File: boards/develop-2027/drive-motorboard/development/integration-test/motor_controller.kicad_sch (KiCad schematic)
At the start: 5 parts

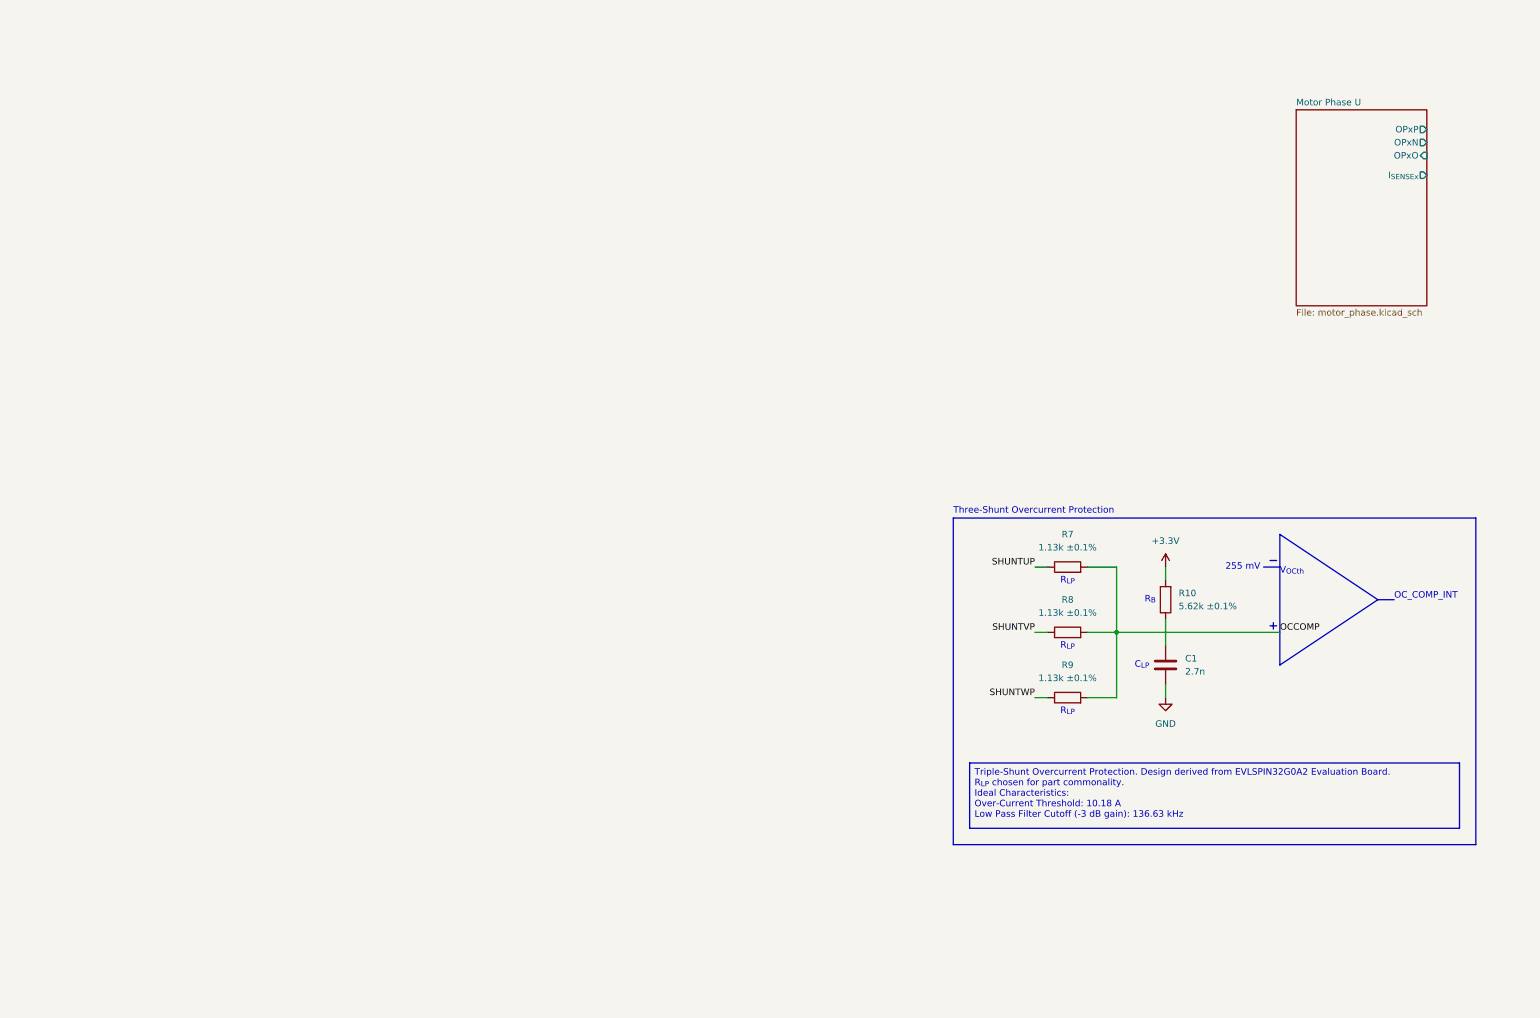
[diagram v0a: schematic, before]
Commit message: Add power stage
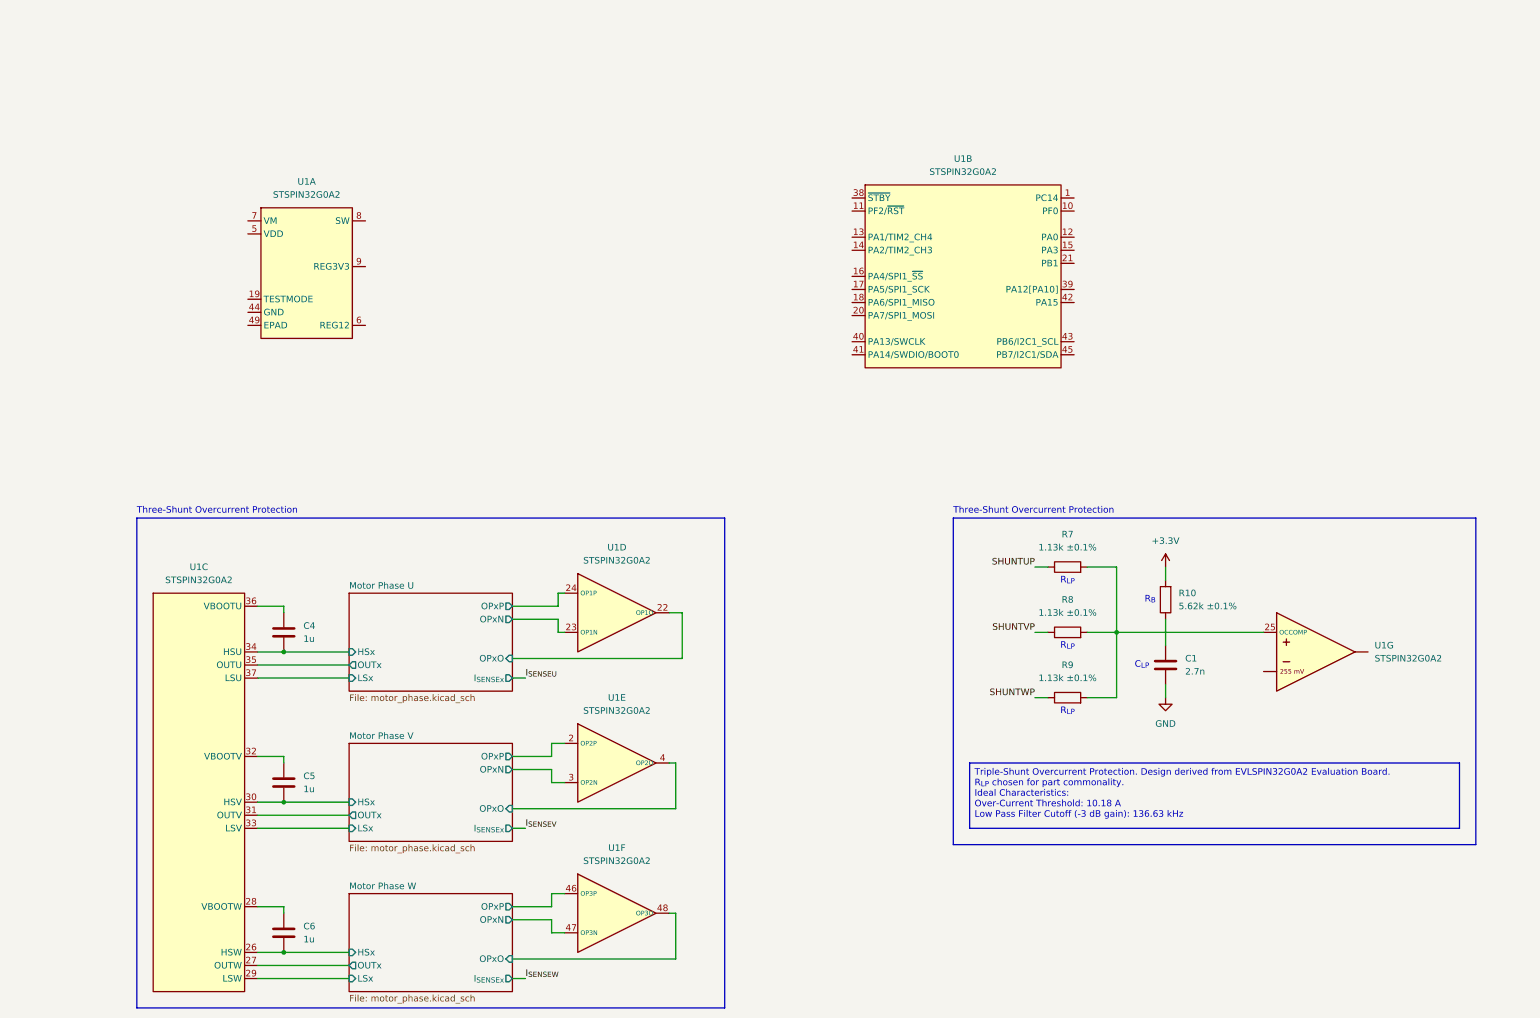
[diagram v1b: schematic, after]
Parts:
- added C4, C5, C6: 1u, Capacitor_SMD:C_0603_1608Metric, symbol Device:C
- added U1: STSPIN32G0A2, Package_DFN_QFN:VQFN-48-1EP_7x7mm_P0.5mm_EP2.6x2.6mm, symbol RJ-MCU:STSPIN32G0A2
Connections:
- net Motor Phase U/OPxN: now also U1.23 (OP1N)
- net Motor Phase U/OPxO: now also U1.22 (OP1O)
- net Motor Phase U/OPxP: now also U1.24 (OP1P)
- net OCCOMP: no longer names the net of R7.2, R8.2, R9.2
- net OCCOMP: now also U1.25 (OCCOMP)
- new net: C6.1, U1.28 (VBOOTW)
- new net: C5.1, U1.32 (VBOOTV)
- new net: C4.1, U1.36 (VBOOTU)
- new net Motor Phase U/HSx: C4.2, U1.34 (HSU)
- new net Motor Phase U/LSx: U1.37 (LSU)
- new net Motor Phase U/OUTx: U1.35 (OUTU)
- new net Motor Phase V/HSx: C5.2, U1.30 (HSV)
- new net Motor Phase V/LSx: U1.33 (LSV)
- new net Motor Phase V/OPxN: U1.3 (OP2N)
- new net Motor Phase V/OPxO: U1.4 (OP2O)
- new net Motor Phase V/OPxP: U1.2 (OP2P)
- new net Motor Phase V/OUTx: U1.31 (OUTV)
- new net Motor Phase W/HSx: C6.2, U1.26 (HSW)
- new net Motor Phase W/LSx: U1.29 (LSW)
- new net Motor Phase W/OPxN: U1.47 (OP3N)
- new net Motor Phase W/OPxO: U1.48 (OP3O)
- new net Motor Phase W/OPxP: U1.46 (OP3P)
- new net Motor Phase W/OUTx: U1.27 (OUTW)
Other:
- added sheet Motor Phase V (motor_phase.kicad_sch)
- added sheet Motor Phase W (motor_phase.kicad_sch)
- sheet Motor Phase U ports: added HSx, LSx, OUTx; removed none
- note removed: "255 mV"
- note removed: "OC_COMP_INT"
- note removed: "V_{OCth}"

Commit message: Add test points
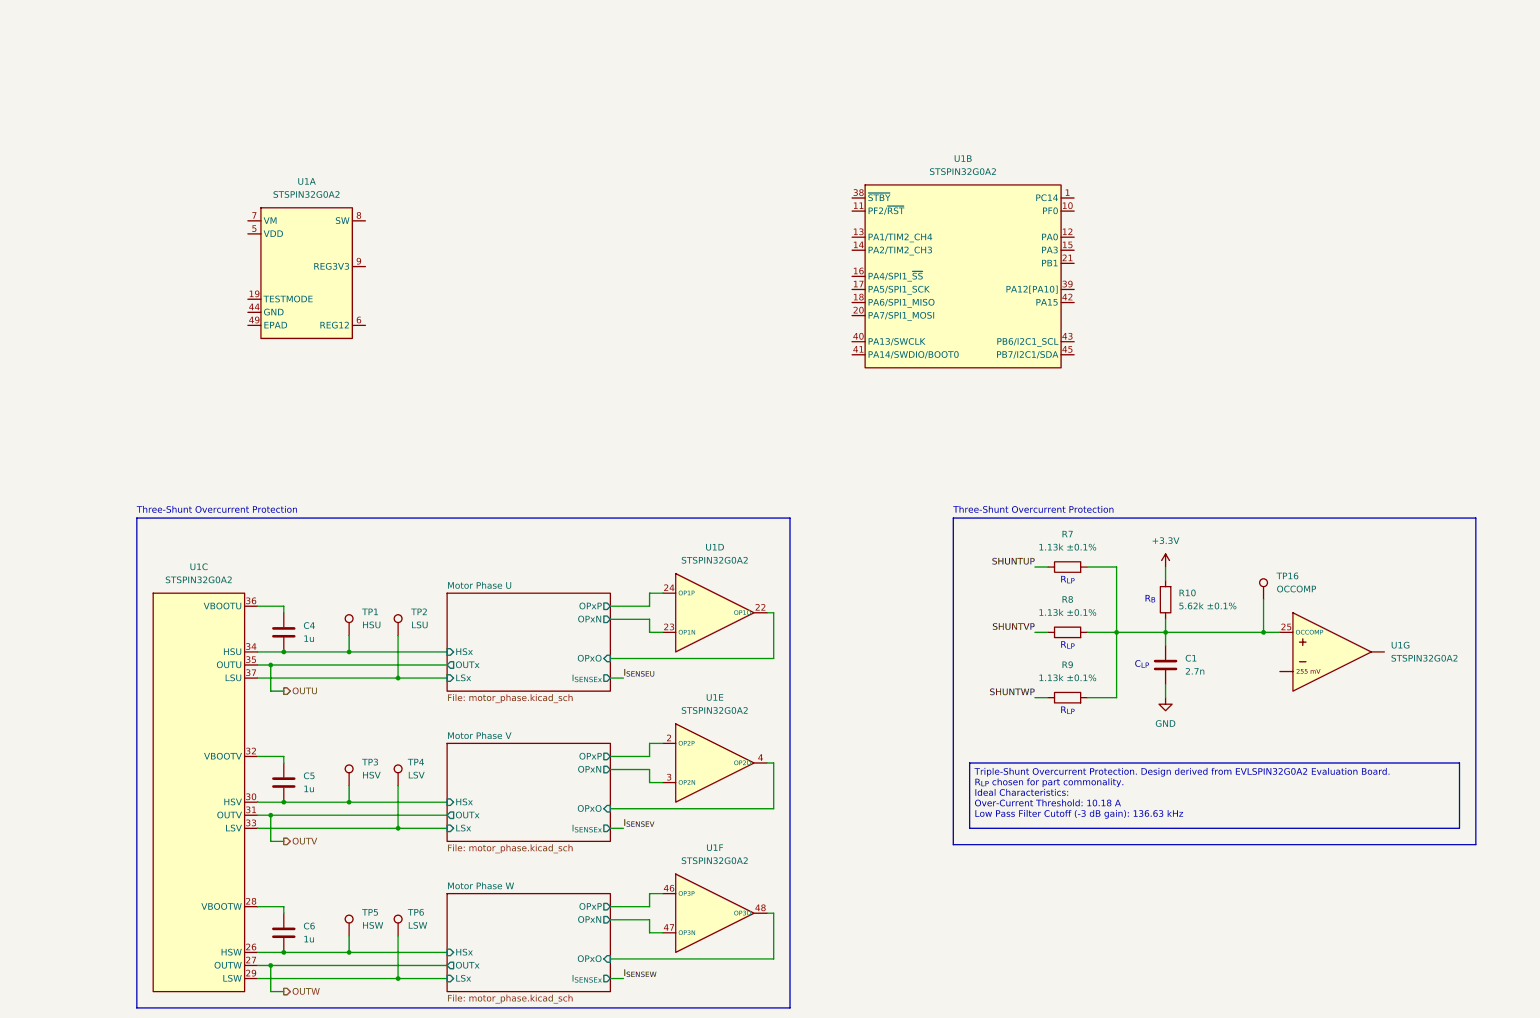
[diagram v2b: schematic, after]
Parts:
- added TP1: HSU, TestPoint:TestPoint_Loop_D1.80mm_Drill1.0mm_Beaded, symbol Connector:TestPoint
- added TP16: OCCOMP, TestPoint:TestPoint_Loop_D1.80mm_Drill1.0mm_Beaded, symbol Connector:TestPoint
- added TP2: LSU, TestPoint:TestPoint_Loop_D1.80mm_Drill1.0mm_Beaded, symbol Connector:TestPoint
- added TP3: HSV, TestPoint:TestPoint_Loop_D1.80mm_Drill1.0mm_Beaded, symbol Connector:TestPoint
- added TP4: LSV, TestPoint:TestPoint_Loop_D1.80mm_Drill1.0mm_Beaded, symbol Connector:TestPoint
- added TP5: HSW, TestPoint:TestPoint_Loop_D1.80mm_Drill1.0mm_Beaded, symbol Connector:TestPoint
- added TP6: LSW, TestPoint:TestPoint_Loop_D1.80mm_Drill1.0mm_Beaded, symbol Connector:TestPoint
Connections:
- net Motor Phase U/HSx: now also TP1.1
- net Motor Phase U/LSx: now also TP2.1
- net Motor Phase V/HSx: now also TP3.1
- net Motor Phase V/LSx: now also TP4.1
- net Motor Phase W/HSx: now also TP5.1
- net Motor Phase W/LSx: now also TP6.1
- net at C1.1, R10.1: now also R7.2, R8.2, R9.2, U1.25 (OCCOMP), TP16.1
- net Motor Phase U/OUTx renamed OUTU
- net Motor Phase V/OUTx renamed OUTV
- net Motor Phase W/OUTx renamed OUTW
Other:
- moved on the sheet: U1D, U1E, U1F, U1G

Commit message: Finish motor controller section
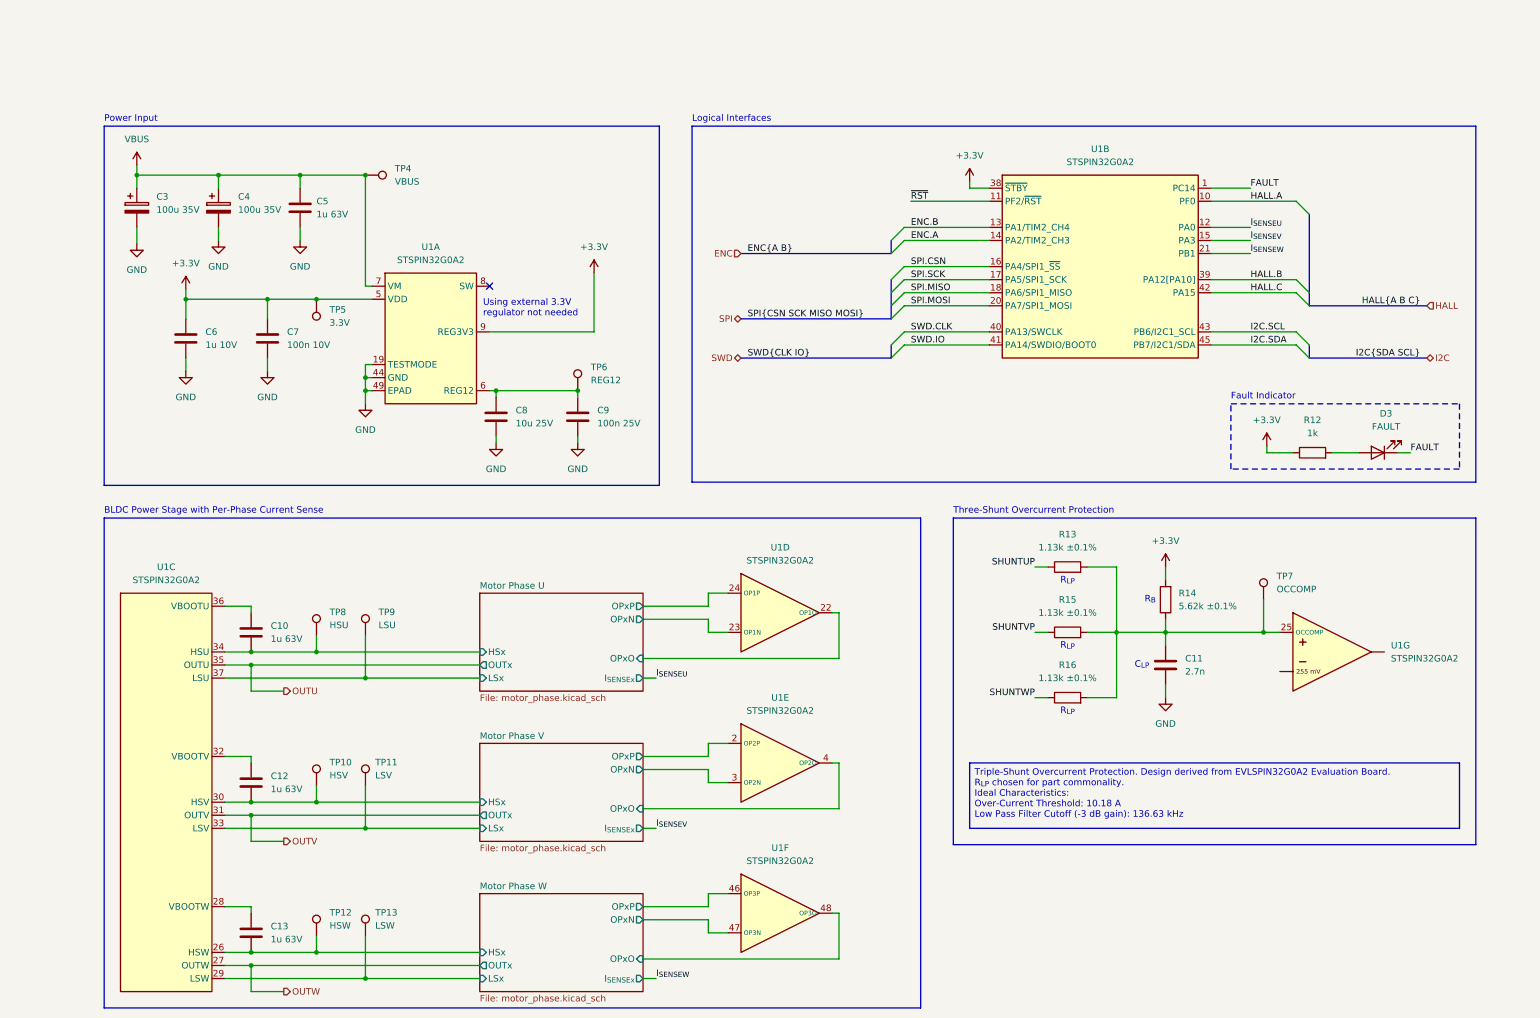
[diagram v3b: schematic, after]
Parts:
- added C3, C4: 100u 35V, Capacitor_SMD:C_Elec_6.3x5.8, symbol Device:C_Polarized
- added C5: 1u 63V, Capacitor_SMD:C_0805_2012Metric, symbol Device:C
- added C6: 1u 10V, Capacitor_SMD:C_0402_1005Metric, symbol Device:C
- added C7: 100n 10V, Capacitor_SMD:C_0402_1005Metric, symbol Device:C
- added C8: 10u 25V, Capacitor_SMD:C_0603_1608Metric, symbol Device:C
- added C9: 100n 25V, Capacitor_SMD:C_0402_1005Metric, symbol Device:C
- added D3: FAULT, LED_SMD:LED_0603_1608Metric, symbol Device:LED
- added R12: 1k, symbol Device:R
- added TP4: VBUS, TestPoint:TestPoint_Loop_D1.80mm_Drill1.0mm_Beaded, symbol Connector:TestPoint
- added TP5: 3.3V, TestPoint:TestPoint_Loop_D1.80mm_Drill1.0mm_Beaded, symbol Connector:TestPoint
- added TP6: REG12, TestPoint:TestPoint_Loop_D1.80mm_Drill1.0mm_Beaded, symbol Connector:TestPoint
- C10: renamed from C4; value 1u -> 1u 63V; footprint Capacitor_SMD:C_0603_1608Metric -> Capacitor_SMD:C_0402_1005Metric
- C12: renamed from C5; value 1u -> 1u 63V; footprint Capacitor_SMD:C_0603_1608Metric -> Capacitor_SMD:C_0402_1005Metric
- C13: renamed from C6; value 1u -> 1u 63V; footprint Capacitor_SMD:C_0603_1608Metric -> Capacitor_SMD:C_0402_1005Metric
- renumbered C1 to C11, R7 to R13, R10 to R14, R8 to R15, R9 to R16, TP3 to TP10, TP4 to TP11, TP5 to TP12, TP6 to TP13, TP16 to TP7, TP1 to TP8, TP2 to TP9
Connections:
- net +3.3V: now also U1.38 (~{STBY}), U1.5 (VDD), U1.9 (REG3V3), C6.1, C7.1, R12.1, TP5.1
- net GND: now also U1.19 (TESTMODE), U1.44 (GND), U1.49 (EPAD), C3.2, C4.2, C5.2, C6.2, C7.2, C8.2, C9.2
- net I_{SENSEU}: now also U1.12 (PA0)
- net I_{SENSEV}: now also U1.15 (PA3)
- net I_{SENSEW}: now also U1.21 (PB1)
- net FAULT: now reaches U1.1 (PC14)
- net FAULT: now also D3.1 (K)
- net HALL.A: now reaches U1.10 (PF0)
- net ~{RST}: now reaches U1.11 (PF2/~{RST})
- net ENC.B: now reaches U1.13 (PA1/TIM2_CH4)
- net ENC.A: now reaches U1.14 (PA2/TIM2_CH3)
- net SPI.CSN: now reaches U1.16 (PA4/SPI1_~{SS})
- net SPI.SCK: now reaches U1.17 (PA5/SPI1_SCK)
- net SPI.MISO: now reaches U1.18 (PA6/SPI1_MISO)
- net SPI.MOSI: now reaches U1.20 (PA7/SPI1_MOSI)
- net HALL.B: now reaches U1.39 (PA12[PA10])
- net SWD.CLK: now reaches U1.40 (PA13/SWCLK)
- net SWD.IO: now reaches U1.41 (PA14/SWDIO/BOOT0)
- net HALL.C: now reaches U1.42 (PA15)
- net I2C.SCL: now reaches U1.43 (PB6/I2C1_SCL)
- net I2C.SDA: now reaches U1.45 (PB7/I2C1/SDA)
- net at U1.6 (REG12): now also C8.1, C9.1, TP6.1
- net VBUS: now reaches U1.7 (VM)
- net VBUS: now also C3.1, C4.1, C5.1, TP4.1
- new net: D3.2 (A), R12.2
- no-connect marks 0 -> 1
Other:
- note added: "BLDC Power Stage with Per-Phase Current Sense"
- note added: "Fault Indicator"
- note added: "Logical Interfaces"
- note added: "Power Input"
- note added: "Using external 3.3V regulator not needed"
- moved on the sheet: C10, C12, C13, TP10, TP11, TP12, TP13, TP8, TP9, U1A, U1B, U1C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

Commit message: Added power and connectors
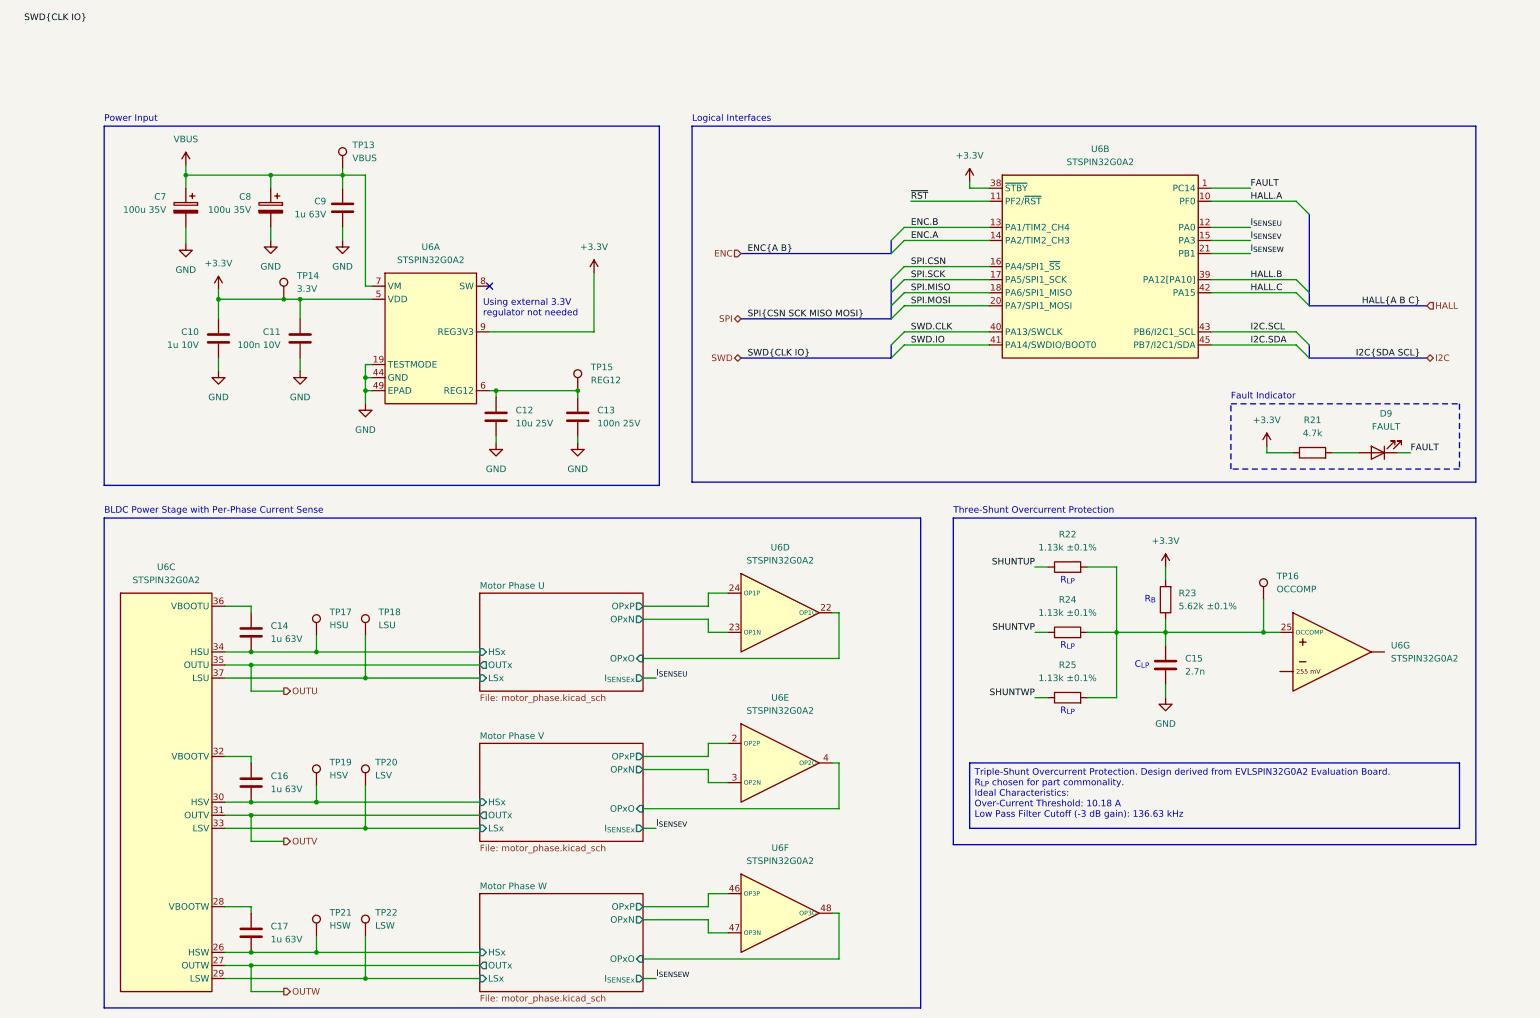
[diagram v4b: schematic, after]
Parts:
- removed R12: 1k, symbol Device:R
- added R21: 4.7k, Resistor_SMD:R_0402_1005Metric, symbol Device:R
- renumbered C6 to C10, C7 to C11, C8 to C12, C9 to C13, C10 to C14, C11 to C15, C12 to C16, C13 to C17, C3 to C7, C4 to C8, C5 to C9, D3 to D9, R13 to R22, R14 to R23, R15 to R24, R16 to R25, TP4 to TP13, TP5 to TP14, TP6 to TP15, TP7 to TP16, TP8 to TP17, TP9 to TP18, TP10 to TP19, TP11 to TP20, TP12 to TP21, TP13 to TP22, U1 to U6
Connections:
- net +3.3V: now also R21.1
- net at D9.2 (A): now also R21.2
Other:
- moved on the sheet: C10, C11, C7, C8, C9, TP13, TP14
